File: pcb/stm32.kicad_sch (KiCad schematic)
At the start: 9 parts, among them U1 STM32F072CBUx

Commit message: kb matrix complete, stm32 wiring done
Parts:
- renumbered C7 to C10, C6 to C3, C2 to C4, C4 to C5, C5 to C6, C8 to C7, C9 to C8, C3 to C9, U1 to U2
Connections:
- net R1: now reaches U2.10 (PA0)
- net R2: now reaches U2.11 (PA1)
- net R3: now reaches U2.12 (PA2)
- net R4: now reaches U2.13 (PA3)
- net R5: now reaches U2.14 (PA4)
- net R6: now reaches U2.15 (PA5)
- net C1: now reaches U2.18 (PB0)
- net C2: now reaches U2.19 (PB1)
- net C17: now reaches U2.2 (PC13)
- net C3: now reaches U2.20 (PB2)
- net C11: now reaches U2.21 (PB10)
- net C12: now reaches U2.22 (PB11)
- net C13: now reaches U2.25 (PB12)
- net C14: now reaches U2.26 (PB13)
- net C15: now reaches U2.27 (PB14)
- net C16: now reaches U2.28 (PB15)
- net C4: now reaches U2.39 (PB3)
- net C5: now reaches U2.40 (PB4)
- net C6: now reaches U2.41 (PB5)
- net C7: now reaches U2.42 (PB6)
- net C8: now reaches U2.43 (PB7)
- net C9: now reaches U2.45 (PB8)
- net C10: now reaches U2.46 (PB9)

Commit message: replaced usb c with molex for udb
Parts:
- added C1: 0.1uF, Capacitor_SMD:C_0402_1005Metric, symbol Device:C
- added R1: 10K, Resistor_SMD:R_0402_1005Metric, symbol Device:R_US
- added TP1: TestPoint, TestPoint:TestPoint_Pad_D1.0mm, symbol Connector:TestPoint
- C7: renamed from C8; footprint Capacitor_SMD:C_0603_1608Metric -> Capacitor_SMD:C_0402_1005Metric
- U1: renamed from U2; Manufacturer Product Number STM32F072CBU6 -> STM32F072CBU7
- renumbered C3 to C2, C4 to C3, C5 to C4, C6 to C5, C7 to C6, C9 to C8, C10 to C9
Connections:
- net GND: now also U1.49 (GND), C1.2, R1.2; no longer U1.EP (GND)
- net BOOT0: now reaches U1.44 (BOOT0)
- net BOOT0: now also R1.1
- net NRST: now reaches U1.7 (NRST)
- net NRST: now also C1.1, TP1.1

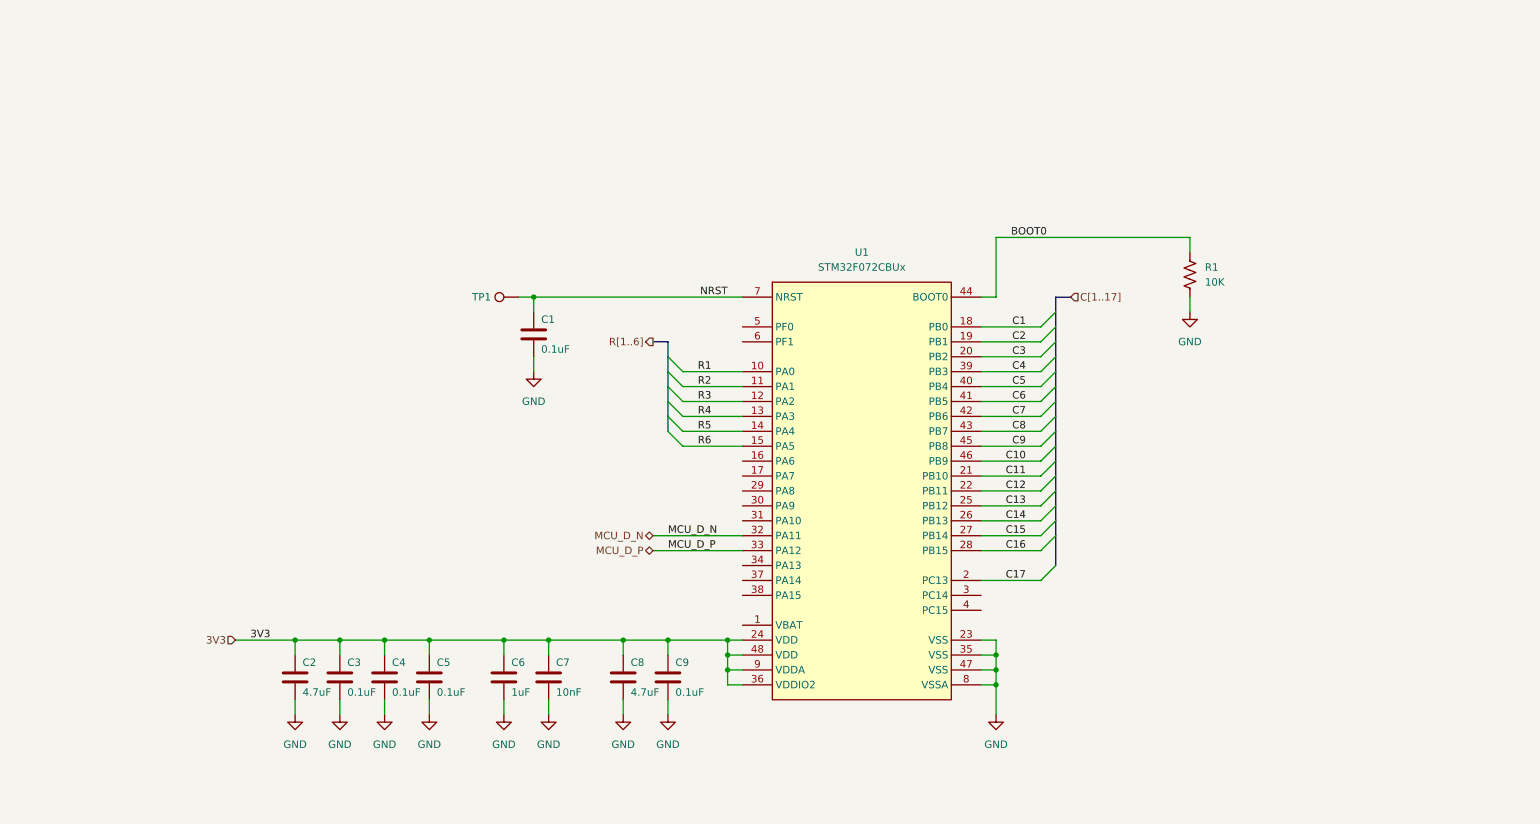
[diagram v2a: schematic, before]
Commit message: reroute matrix
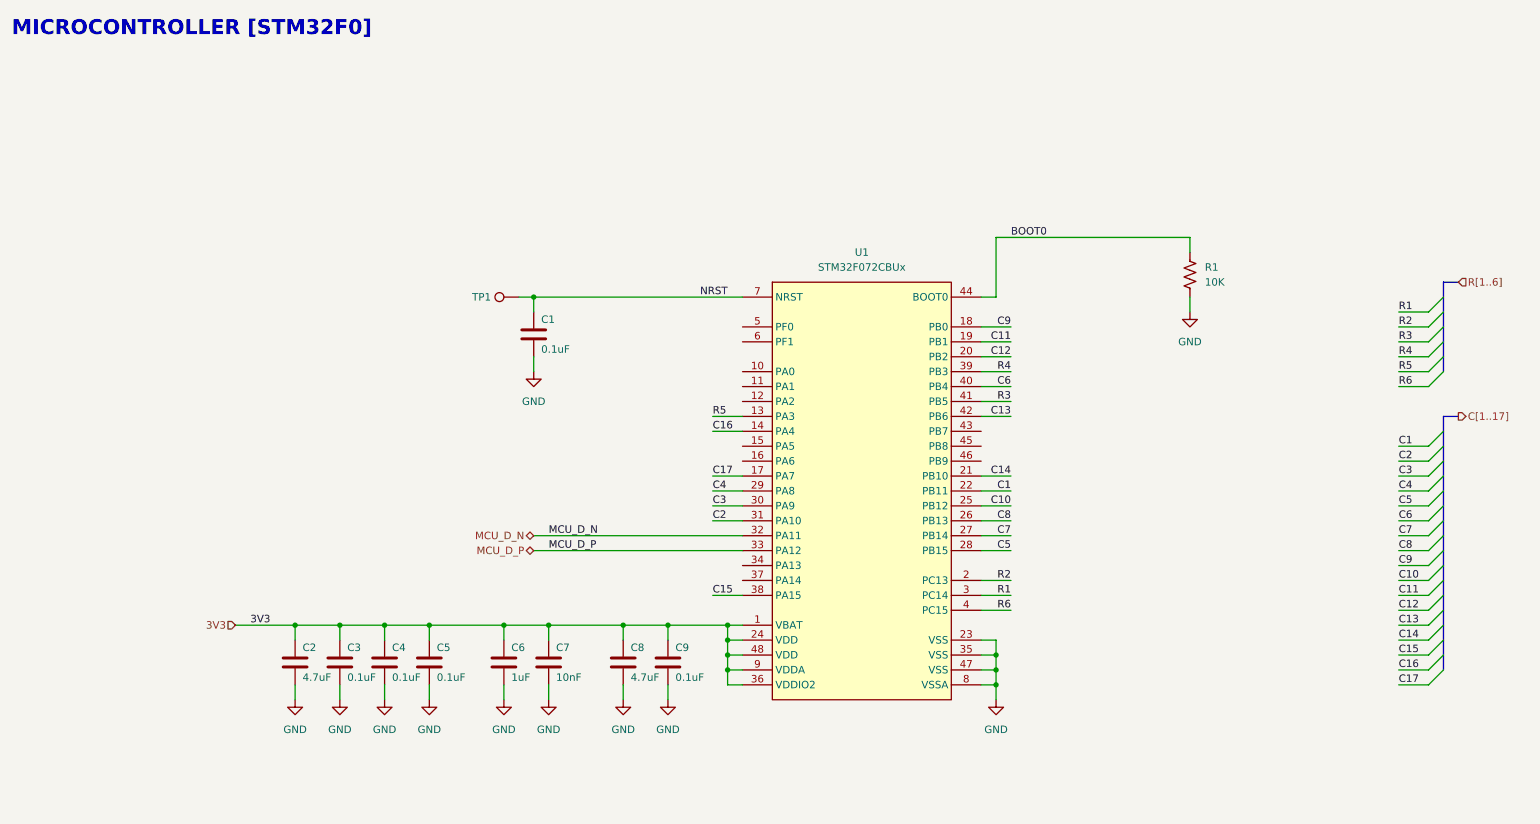
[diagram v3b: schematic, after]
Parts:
- C6: footprint Capacitor_SMD:C_0402_1005Metric -> Capacitor_SMD:C_0603_1608Metric; Manufacturer Product Number C0402C105K9PACTU -> C0603C105K4RACTU
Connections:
- net 3V3: now also U1.1 (VBAT)
- net C1: now also U1.22 (PB11); no longer U1.18 (PB0)
- net C10: now also U1.25 (PB12); no longer U1.46 (PB9)
- net C11: now also U1.19 (PB1); no longer U1.21 (PB10)
- net C12: now also U1.20 (PB2); no longer U1.22 (PB11)
- net C13: now also U1.42 (PB6); no longer U1.25 (PB12)
- net C14: now also U1.21 (PB10); no longer U1.26 (PB13)
- net C15: now also U1.38 (PA15); no longer U1.27 (PB14)
- net C16: now also U1.14 (PA4); no longer U1.28 (PB15)
- net C17: now also U1.17 (PA7); no longer U1.2 (PC13)
- net C2: now also U1.31 (PA10); no longer U1.19 (PB1)
- net C3: now also U1.30 (PA9); no longer U1.20 (PB2)
- net C4: now also U1.29 (PA8); no longer U1.39 (PB3)
- net C5: now also U1.28 (PB15); no longer U1.40 (PB4)
- net C6: now also U1.40 (PB4); no longer U1.41 (PB5)
- net C7: now also U1.27 (PB14); no longer U1.42 (PB6)
- net C8: now also U1.26 (PB13); no longer U1.43 (PB7)
- net C9: now also U1.18 (PB0); no longer U1.45 (PB8)
- net R1: now also U1.3 (PC14); no longer U1.10 (PA0)
- net R2: now also U1.2 (PC13); no longer U1.11 (PA1)
- net R3: now also U1.41 (PB5); no longer U1.12 (PA2)
- net R4: now also U1.39 (PB3); no longer U1.13 (PA3)
- net R5: now also U1.13 (PA3); no longer U1.14 (PA4)
- net R6: now also U1.4 (PC15); no longer U1.15 (PA5)
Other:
- note added: "MICROCONTROLLER [STM32F0]"
- company: (none) -> ASE, ASW, AMB
- title: (none) -> ALANA-KB PCB
- moved on the sheet: C2, C3, C4, C5, C6, C7, C8, C9

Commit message: finish layout
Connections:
- net C1: now also U1.14 (PA4); no longer U1.22 (PB11)
- net C10: now also U1.28 (PB15); no longer U1.25 (PB12)
- net C11: now also U1.29 (PA8); no longer U1.19 (PB1)
- net C12: now also U1.22 (PB11); no longer U1.20 (PB2)
- net C13: now also U1.30 (PA9); no longer U1.42 (PB6)
- net C14: now also U1.31 (PA10); no longer U1.21 (PB10)
- net C15: now also U1.16 (PA6); no longer U1.38 (PA15)
- net C16: now also U1.12 (PA2); no longer U1.14 (PA4)
- net C17: now also U1.6 (PF1); no longer U1.17 (PA7)
- net C2: now also U1.15 (PA5); no longer U1.31 (PA10)
- net C3: now also U1.17 (PA7); no longer U1.30 (PA9)
- net C4: now also U1.26 (PB13); no longer U1.29 (PA8)
- net C5: now also U1.27 (PB14); no longer U1.28 (PB15)
- net C6: now also U1.18 (PB0); no longer U1.40 (PB4)
- net C7: now also U1.19 (PB1); no longer U1.27 (PB14)
- net C8: now also U1.20 (PB2); no longer U1.26 (PB13)
- net C9: now also U1.21 (PB10); no longer U1.18 (PB0)
- net R1: now also U1.4 (PC15); no longer U1.3 (PC14)
- net R2: now also U1.3 (PC14); no longer U1.2 (PC13)
- net R3: now also U1.37 (PA14); no longer U1.41 (PB5)
- net R4: now also U1.25 (PB12); no longer U1.39 (PB3)
- net R5: now also U1.11 (PA1); no longer U1.13 (PA3)
- net R6: now also U1.5 (PF0); no longer U1.4 (PC15)
